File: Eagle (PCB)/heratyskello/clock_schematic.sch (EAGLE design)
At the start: 27 parts, among them IC1 DS3231/SO, J1 USB-B-S

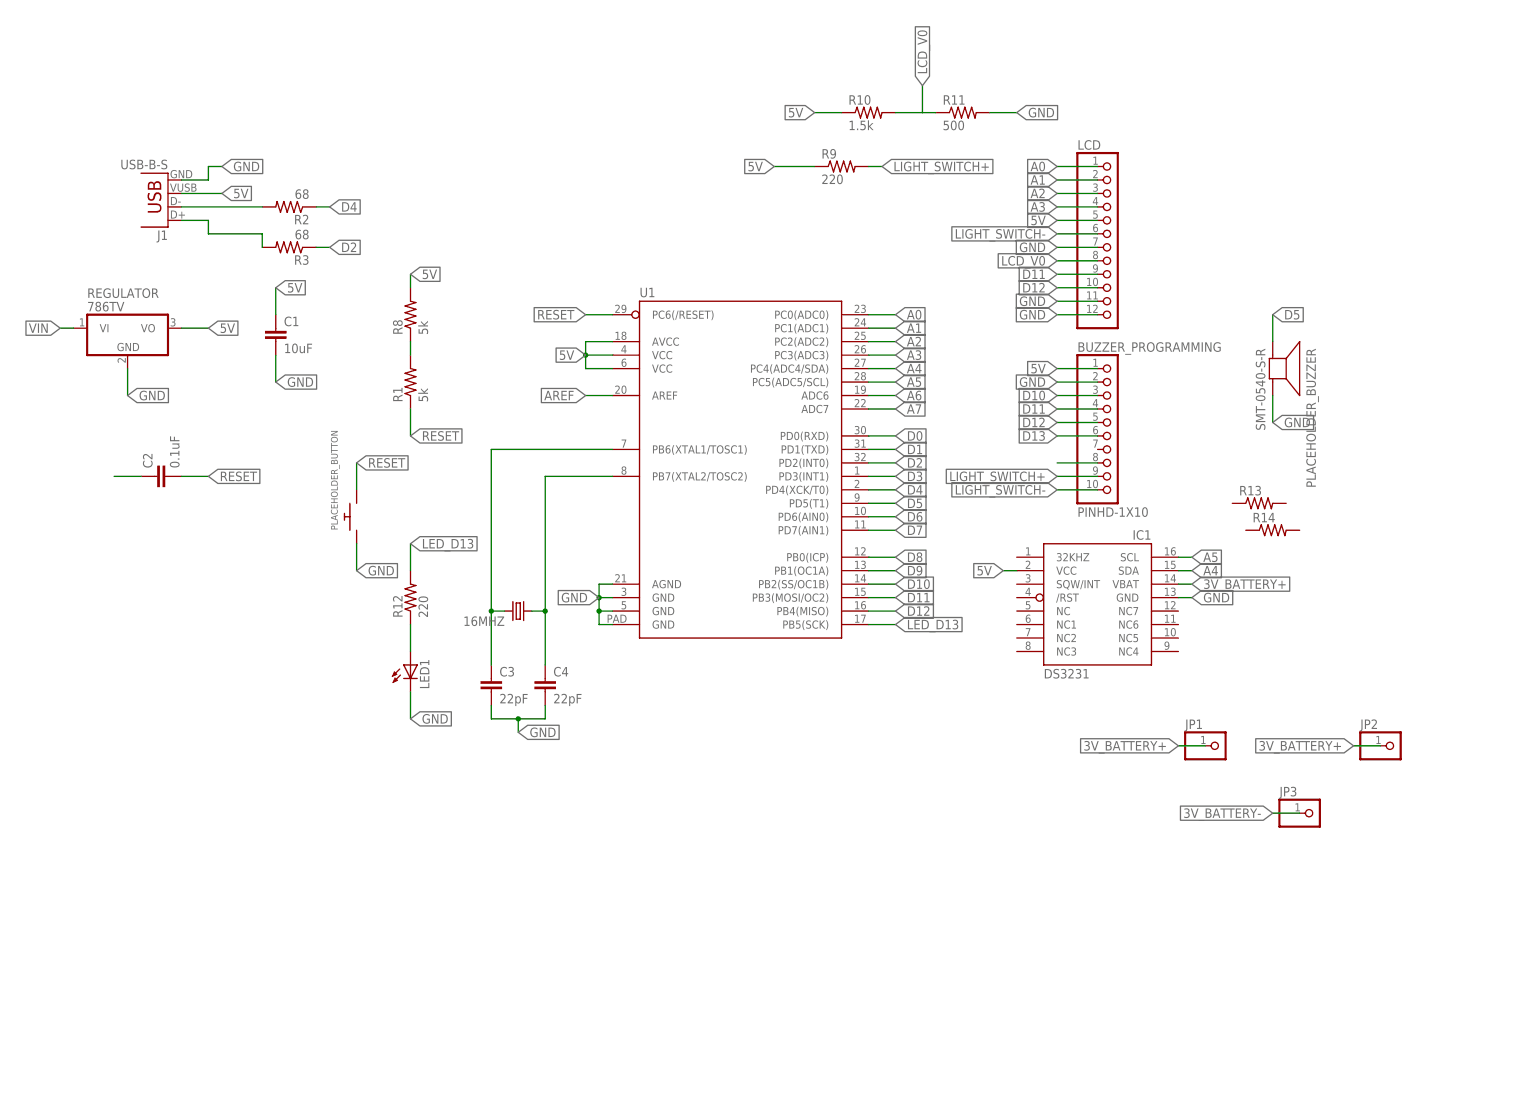
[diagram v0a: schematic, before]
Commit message: Eagle paths almost made
Most of the paths are made. Only regulator replacement needed.
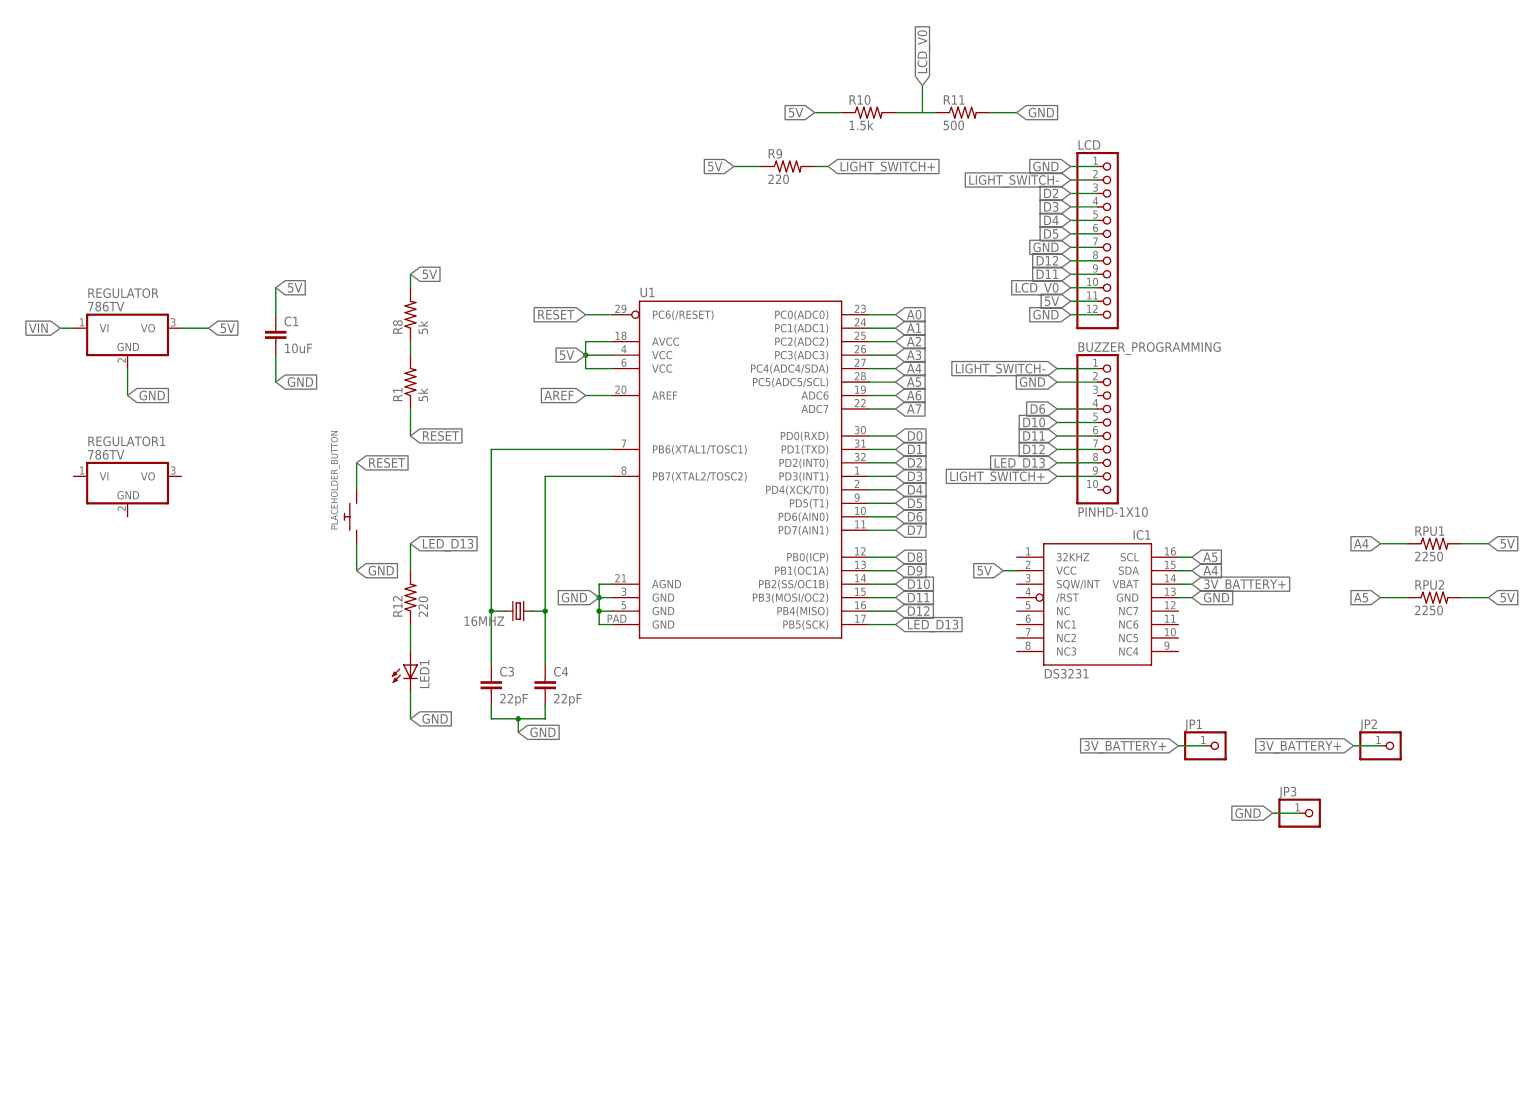
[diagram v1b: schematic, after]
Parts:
- removed C2: 0.1uF, SparkFun-Capacitors:CAP0805
- removed J1: USB-B-S, SparkFun-Connectors:USB-B-S
- removed PLACEHOLDER_BUZZER: SMT-0540-S-R, adafruit:SMT-0540-S-R
- removed R13, R14: (no value), SparkFun-Resistors:RESISTOR0805-RES
- removed R2, R3: 68, SparkFun-Resistors:RESISTOR0805-RES
- added REGULATOR1: 786TV, linear:786TV
- added RPU1, RPU2: 2250, SparkFun-Resistors:RESISTOR0805-RES
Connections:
- removed net 3V_BATTERY-: JP3.1
- removed net D13: BUZZER_PROGRAMMING.6
- removed net N$23: BUZZER_PROGRAMMING.8
- removed net N$31: C2.1
- removed net N$33: J1.D-, R2.2
- removed net N$34: J1.D+, R3.2
- net 5V: now also LCD.11, RPU1.2, RPU2.2; no longer BUZZER_PROGRAMMING.1, J1.VBUS, LCD.5
- net A0: no longer LCD.1
- net A1: no longer LCD.2
- net A2: no longer LCD.3
- net A3: no longer LCD.4
- net A4: now also RPU1.1
- net A5: now also RPU2.1
- net D10: now also BUZZER_PROGRAMMING.5; no longer BUZZER_PROGRAMMING.3
- net D11: now also BUZZER_PROGRAMMING.6; no longer BUZZER_PROGRAMMING.4
- net D12: now also BUZZER_PROGRAMMING.7, LCD.8; no longer BUZZER_PROGRAMMING.5, LCD.10
- net D2: now also LCD.3; no longer R3.1
- net D3: now also LCD.4
- net D4: now also LCD.5; no longer R2.1
- net D5: now also LCD.6; no longer PLACEHOLDER_BUZZER.+
- net D6: now also BUZZER_PROGRAMMING.4
- net GND: now also JP3.1, LCD.1; no longer J1.GND, LCD.11, PLACEHOLDER_BUZZER.-
- net LCD_V0: now also LCD.10; no longer LCD.8
- net LED_D13: now also BUZZER_PROGRAMMING.8
- net LIGHT_SWITCH-: now also BUZZER_PROGRAMMING.1, LCD.2; no longer BUZZER_PROGRAMMING.10, LCD.6
- net RESET: no longer C2.2
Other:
- moved on the sheet: R9

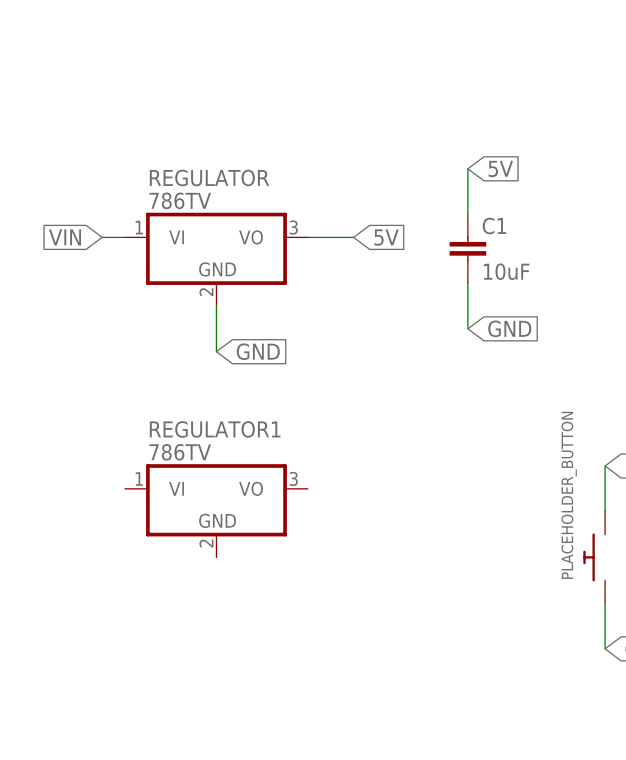
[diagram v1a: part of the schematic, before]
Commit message: Eagle File Complete
Regulator was moved to make the PCB smaller. Also moved the 5V connection that was under the 3V battery case lower so it wouldn't be left under the battery.
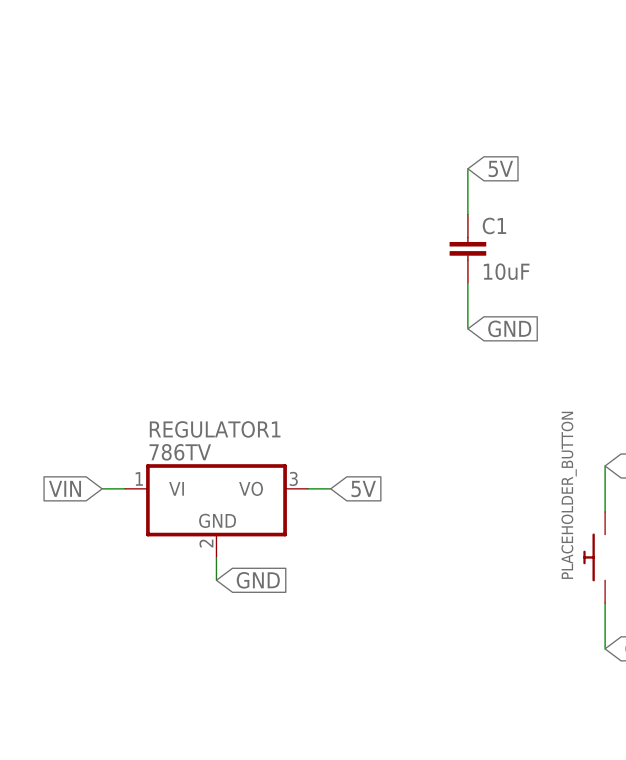
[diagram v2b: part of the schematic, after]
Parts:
- removed REGULATOR: 786TV, linear:786TV
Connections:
- net 5V: now also REGULATOR1.VO; no longer REGULATOR.VO
- net GND: now also REGULATOR1.GND; no longer REGULATOR.GND
- net VIN: now also REGULATOR1.VI; no longer REGULATOR.VI
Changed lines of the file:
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@@
 <part name="R1" library="SparkFun-Resistors" deviceset="RESISTOR" device="0805-RES" value="5k"/>
 <part name="C1" library="SparkFun-Capacitors" deviceset="CAP" device="0805" value="10uF"/>
-<part name="REGULATOR" library="linear" deviceset="78*" device="TV" technology="6"/>
 <part name="BUZZER_PROGRAMMING" library="adafruit" deviceset="PINHD-1X10" device=""/>
 <part name="PLACEHOLDER_BUTTON" library="adafruit" deviceset="SWITCH_PUSHBUTTON" device="SOFTTOUCHSMD_SJ"/>
@@
 <instance part="R1" gate="G$1" x="-63.5" y="86.36" rot="R90"/>
 <instance part="C1" gate="G$1" x="-88.9" y="93.98"/>
-<instance part="REGULATOR" gate="A1" x="-116.84" y="96.52"/>
 <instance part="BUZZER_PROGRAMMING" gate="G$1" x="68.58" y="78.74"/>
 <instance part="PLACEHOLDER_BUTTON" gate="G$1" x="-73.66" y="60.96" rot="R90"/>
@@
 </segment>
 <segment>
-<pinref part="REGULATOR" gate="A1" pin="GND"/>
-<wire x1="-116.84" y1="88.9" x2="-116.84" y2="83.82" width="0.1524" layer="91"/>
-<label x="-116.84" y="83.82" size="1.778" layer="95" xref="yes"/>
-</segment>
-<segment>
 <pinref part="IC1" gate="G$1" pin="GND"/>
 <wire x1="81.28" y1="45.72" x2="83.82" y2="45.72" width="0.1524" layer="91"/>
@@
 <wire x1="66.04" y1="86.36" x2="58.42" y2="86.36" width="0.1524" layer="91"/>
 <label x="58.42" y="86.36" size="1.778" layer="95" rot="R180" xref="yes"/>
+</segment>
+<segment>
+<pinref part="REGULATOR1" gate="A1" pin="GND"/>
+<wire x1="-116.84" y1="60.96" x2="-116.84" y2="58.42" width="0.1524" layer="91"/>
+<label x="-116.84" y="58.42" size="1.778" layer="95" xref="yes"/>
 </segment>
 </net>
@@
 </segment>
 <segment>
-<pinref part="REGULATOR" gate="A1" pin="VO"/>
-<wire x1="-106.68" y1="96.52" x2="-101.6" y2="96.52" width="0.1524" layer="91"/>
-<label x="-101.6" y="96.52" size="1.778" layer="95" xref="yes"/>
-</segment>
-<segment>
 <pinref part="R10" gate="G$1" pin="1"/>
 <wire x1="17.78" y1="137.16" x2="12.7" y2="137.16" width="0.1524" layer="91"/>
@@
 <wire x1="134.62" y1="45.72" x2="139.7" y2="45.72" width="0.1524" layer="91"/>
 <label x="139.7" y="45.72" size="1.778" layer="95" xref="yes"/>
+</segment>
+<segment>
+<pinref part="REGULATOR1" gate="A1" pin="VO"/>
+<wire x1="-106.68" y1="68.58" x2="-104.14" y2="68.58" width="0.1524" layer="91"/>
+<label x="-104.14" y="68.58" size="1.778" layer="95" xref="yes"/>
 </segment>
 </net>
@@
 <net name="VIN" class="0">
 <segment>
-<pinref part="REGULATOR" gate="A1" pin="VI"/>
-<wire x1="-127" y1="96.52" x2="-129.54" y2="96.52" width="0.1524" layer="91"/>
-<label x="-129.54" y="96.52" size="1.778" layer="95" rot="R180" xref="yes"/>
-</segment>
-</net>
+<pinref part="REGULATOR1" gate="A1" pin="VI"/>
+<wire x1="-127" y1="68.58" x2="-129.54" y2="68.58" width="0.1524" layer="91"/>
+<label x="-129.54" y="68.58" size="1.778" layer="95" rot="R180" xref="yes"/>
+</segment>
+</net>
